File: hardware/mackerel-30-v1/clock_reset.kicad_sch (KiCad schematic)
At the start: 26 parts, among them J1 Conn_01x03, J2 Conn_01x07, SW1 SW_Push, U1 ATtiny1614-SS, U2 MCP1700x-330xxTO, U3 74AHCT125, U4 74LVC07A, Y1 Si5351A-B-GT, Y2 Crystal_GND24

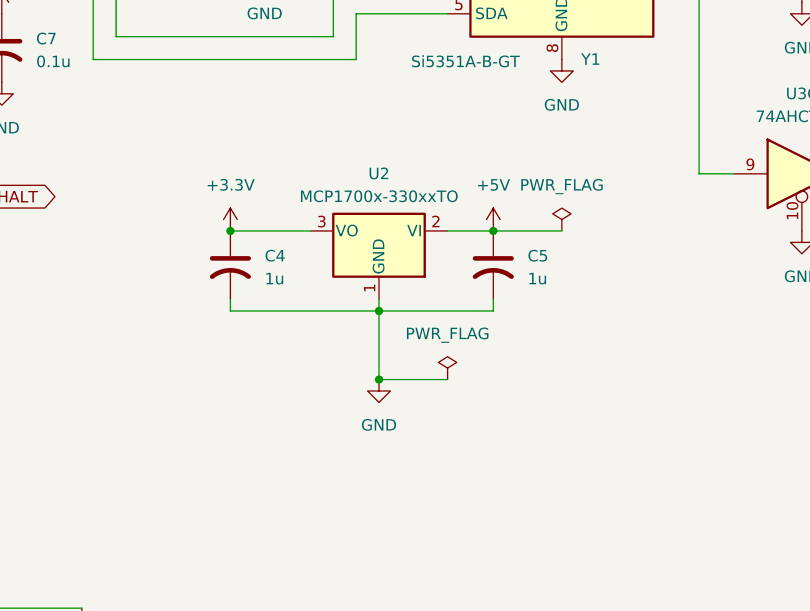
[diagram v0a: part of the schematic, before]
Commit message: Mackerel-30: Add low mem, FPU, DRAM, DUART, IDE, power sheets to schematic
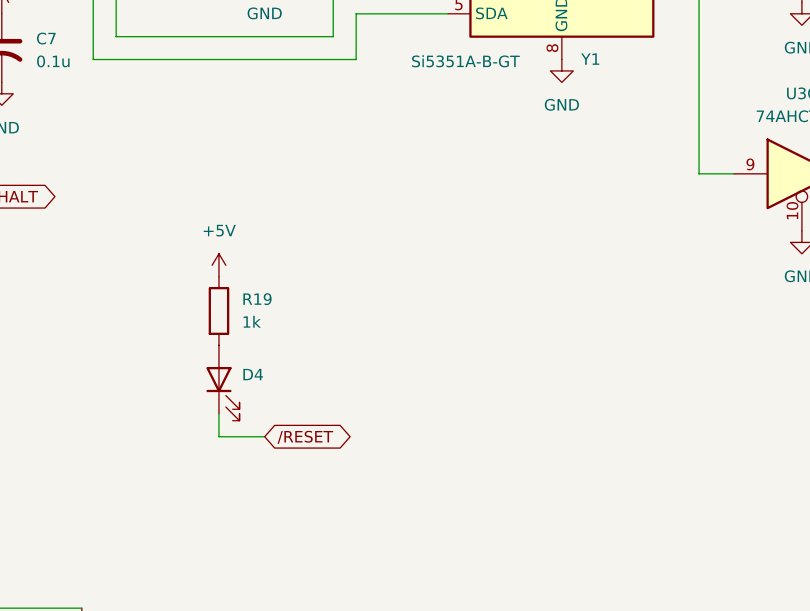
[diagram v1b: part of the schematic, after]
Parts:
- removed C4, C5: 1u, Capacitor_SMD:C_0805_2012Metric_Pad1.18x1.45mm_HandSolder, symbol Device:C_US
- removed U2: MCP1700x-330xxTO, Package_TO_SOT_THT:TO-92_Inline, symbol Regulator_Linear:MCP1700x-330xxTO
- added D4: LED, LED_THT:LED_D5.0mm, symbol Device:LED
- added R19: 1k, Resistor_THT:R_Axial_DIN0207_L6.3mm_D2.5mm_P7.62mm_Horizontal, symbol Device:R
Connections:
- net +5V: now also R19.1
- net /RESET: now also D4.1 (K)
- new net: D4.2 (A), R19.2
